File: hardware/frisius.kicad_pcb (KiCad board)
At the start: 2 copper layers, 40 x 60 mm, 17 parts

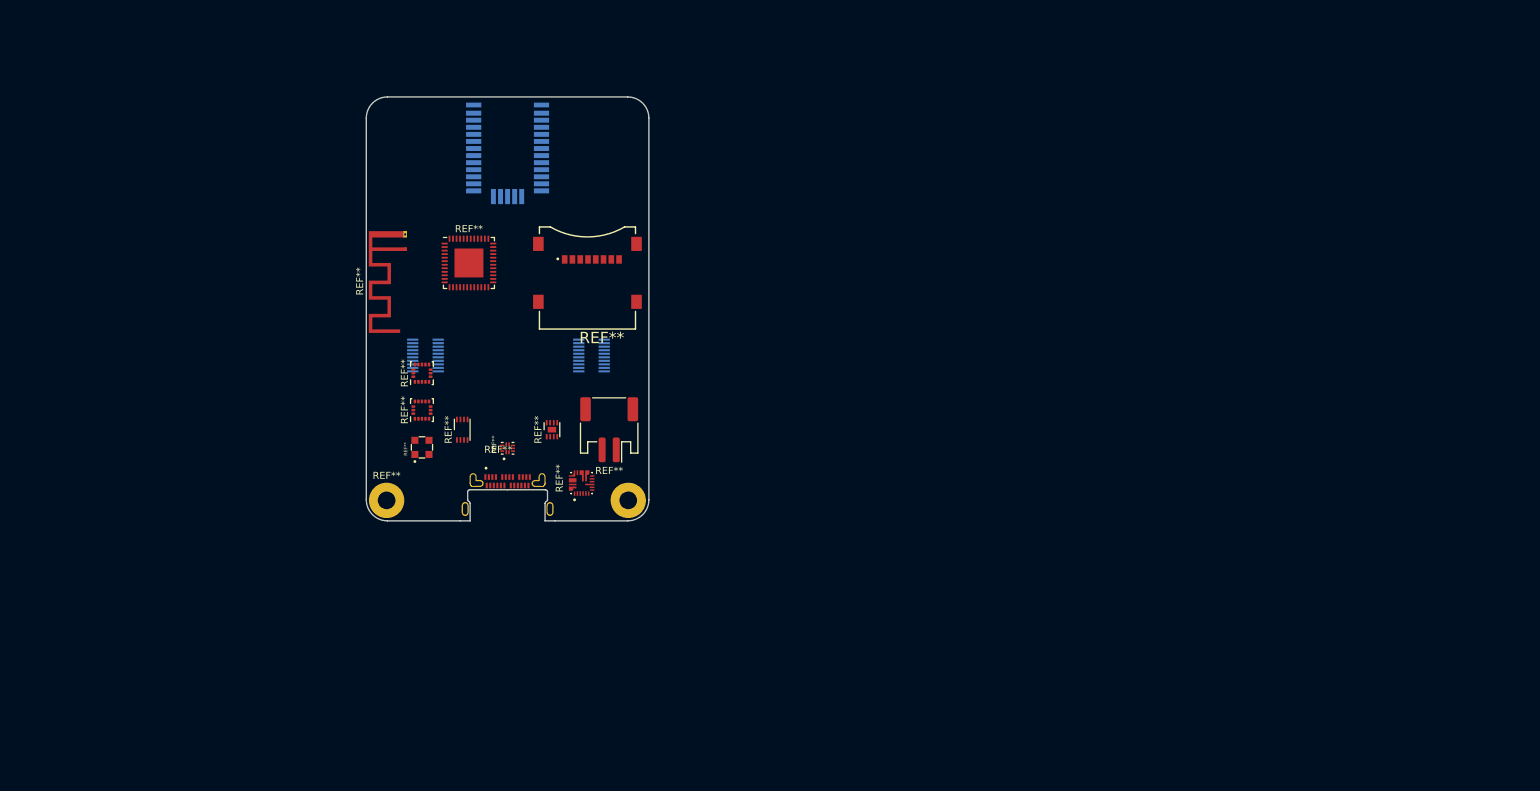
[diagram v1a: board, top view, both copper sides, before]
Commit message: checking footprint assignment, added current sense pac1934 for dev
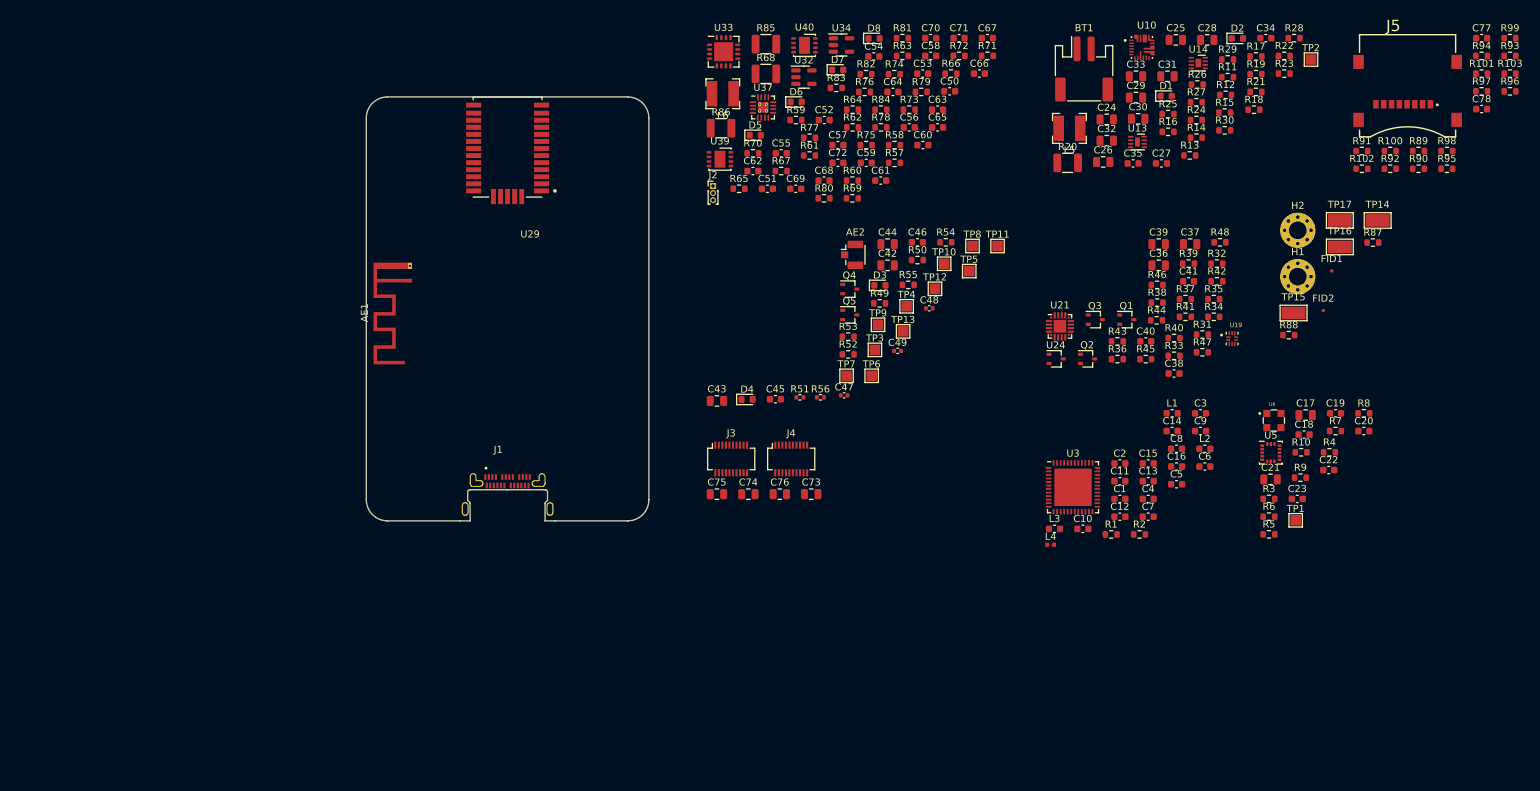
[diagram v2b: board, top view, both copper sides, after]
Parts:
- removed ?: , 
- removed REF**: DFN-8-1EP_3x2mm_P0.5mm_EP1.7x1.4mm, Package_DFN_QFN:DFN-8-1EP_3x2mm_P0.5mm_EP1.7x1.4mm
- removed REF** (x2): LGA-16_3x3mm_P0.5mm_LayoutBorder3x5y, Package_LGA:LGA-16_3x3mm_P0.5mm_LayoutBorder3x5y
- removed REF**: VQFN-48-1EP_7x7mm_P0.5mm_EP4.1x4.1mm, Package_DFN_QFN:VQFN-48-1EP_7x7mm_P0.5mm_EP4.1x4.1mm
- removed REF**: IC_MAX77751CEFG+, Package_QFN_bt:FC2QFN-24-3x3_P0.4mm
- removed REF**: IC_FSUSB30UMX, Package_QFN_bt:UMLP-10-1.4x1.8_P0.4mm
- removed REF**: XCVR_L96-M33, Module_GPS_bt:Quectel_L96-M33
- removed REF** (x2): Hirose_DF12_DF12E3.0-20DP-0.5V_2x10_P0.50mm_Vertical, Connector_Hirose:Hirose_DF12_DF12E3.0-20DP-0.5V_2x10_P0.50mm_Vertical
- removed REF**: AMPHENOL_124019032112A, Connector_USB_bt:AMPHENOL_124019032112A
- removed REF**: Texas_SWRA117D_2.4GHz_Left, RF_Antenna:Texas_SWRA117D_2.4GHz_Left
- removed REF**: TDFN-8-1EP_2x2mm_P0.5mm_EP0.8x1.2mm, Package_DFN_QFN:TDFN-8-1EP_2x2mm_P0.5mm_EP0.8x1.2mm
- removed REF**: TE_MS563702BA03-50, Package_LGA_bt:TE_MS563702BA03-50
- removed REF**: GCT_MEM2067-02-180-00-A_REVB, Connector_uSD_bt:GCT_MEM2067-02-180-00-A_REVB
- removed REF**: JST_PH_S2B-PH-SM4-TB_1x02-1MP_P2.00mm_Horizontal, Connector_JST:JST_PH_S2B-PH-SM4-TB_1x02-1MP_P2.00mm_Horizontal
- removed REF**: MountingHole_2.5mm_Pad, MountingHole:MountingHole_2.5mm_Pad
- added AE1: 2.4G, RF_Antenna:Texas_SWRA117D_2.4GHz_Left, F.Cu at (120.8, 59.9)
- added AE2: GPS_EXT, Connector_Coaxial:U.FL_Hirose_U.FL-R-SMT-1_Vertical, F.Cu at (183.4, 56.2)
- added BT1: JST-PH-2, Connector_JST:JST_PH_S2B-PH-SM4-TB_1x02-1MP_P2.00mm_Horizontal, F.Cu at (216.2, 29.9)
- added C1: 0.1u, Capacitor_SMD:C_0603_1608Metric, F.Cu at (221.3, 90.8)
- added C10: 4.7u, Capacitor_SMD:C_0603_1608Metric, F.Cu at (216.0, 95.0)
- added C11: 4.7u, Capacitor_SMD:C_0603_1608Metric, F.Cu at (221.3, 88.3)
- added C12: 4.7u, Capacitor_SMD:C_0603_1608Metric, F.Cu at (221.3, 93.3)
- added C13: 4.7u, Capacitor_SMD:C_0603_1608Metric, F.Cu at (225.3, 88.3)
- added C14: 4.7u, Capacitor_SMD:C_0603_1608Metric, F.Cu at (228.7, 81.2)
- added C15: 0.1u, Capacitor_SMD:C_0603_1608Metric, F.Cu at (225.3, 85.8)
- added C16: 0.1u, Capacitor_SMD:C_0603_1608Metric, F.Cu at (229.3, 86.2)
- added C17: 4.7u, Capacitor_SMD:C_0805_2012Metric, F.Cu at (247.6, 78.9)
- added C18: 0.1u, Capacitor_SMD:C_0603_1608Metric, F.Cu at (247.3, 81.7)
- added C19: 0.1u, Capacitor_SMD:C_0603_1608Metric, F.Cu at (251.8, 78.7)
- added C2: 0.1u, Capacitor_SMD:C_0603_1608Metric, F.Cu at (221.3, 85.8)
- added C20: 0.1u, Capacitor_SMD:C_0603_1608Metric, F.Cu at (255.8, 81.2)
- added C21: 4.7u, Capacitor_SMD:C_0805_2012Metric, F.Cu at (242.6, 88.0)
- added C22: 0.1u, Capacitor_SMD:C_0603_1608Metric, F.Cu at (250.8, 86.7)
- added C23: 0.1u, Capacitor_SMD:C_0603_1608Metric, F.Cu at (246.4, 90.8)
- added C24: 4.7u, Capacitor_SMD:C_0805_2012Metric, F.Cu at (219.4, 37.1)
- added C25: 4.7u, Capacitor_SMD:C_0805_2012Metric, F.Cu at (229.2, 25.8)
- added C26: 4.7u, Capacitor_SMD:C_0805_2012Metric, F.Cu at (218.9, 43.1)
- added C27: 0.1u, Capacitor_SMD:C_0603_1608Metric, F.Cu at (227.2, 43.3)
- added C28: 4.7u, Capacitor_SMD:C_0805_2012Metric, F.Cu at (233.7, 25.8)
- added C29: 10u, Capacitor_SMD:C_0805_2012Metric, F.Cu at (223.6, 34.0)
- added C3: DNF, Capacitor_SMD:C_0603_1608Metric, F.Cu at (232.7, 78.7)
- added C30: 10u, Capacitor_SMD:C_0805_2012Metric, F.Cu at (223.9, 37.0)
- added C31: 10u, Capacitor_SMD:C_0805_2012Metric, F.Cu at (228.0, 31.0)
- added C32: 10u, Capacitor_SMD:C_0805_2012Metric, F.Cu at (219.4, 40.1)
- added C33: 10u, Capacitor_SMD:C_0805_2012Metric, F.Cu at (223.6, 31.0)
- added C34: 0.1u, Capacitor_SMD:C_0603_1608Metric, F.Cu at (241.9, 25.6)
- added C35: 0.1u, Capacitor_SMD:C_0603_1608Metric, F.Cu at (223.2, 43.3)
- added C36: 4.7u, Capacitor_SMD:C_0805_2012Metric, F.Cu at (226.8, 57.7)
- added C37: 4.7u, Capacitor_SMD:C_0805_2012Metric, F.Cu at (231.2, 54.7)
- added C38: 0.1u, Capacitor_SMD:C_0603_1608Metric, F.Cu at (228.9, 73.0)
- added C39: 4.7u, Capacitor_SMD:C_0805_2012Metric, F.Cu at (226.8, 54.7)
- added C4: DNF, Capacitor_SMD:C_0603_1608Metric, F.Cu at (225.3, 90.8)
- added C40: 0.1u, Capacitor_SMD:C_0603_1608Metric, F.Cu at (224.9, 68.5)
- added C41: 0.1u, Capacitor_SMD:C_0603_1608Metric, F.Cu at (231.0, 60.0)
- added C42: 4.7u, Capacitor_SMD:C_0805_2012Metric, F.Cu at (188.4, 57.7)
- added C43: 4.7u, Capacitor_SMD:C_0805_2012Metric, F.Cu at (164.2, 76.9)
- added C44: 4.7u, Capacitor_SMD:C_0805_2012Metric, F.Cu at (188.4, 54.7)
- added C45: 0.1u, Capacitor_SMD:C_0603_1608Metric, F.Cu at (172.5, 76.7)
- added C46: 0.1u, Capacitor_SMD:C_0603_1608Metric, F.Cu at (192.6, 54.5)
- added C47: DNF, Capacitor_SMD:C_0402_1005Metric, F.Cu at (182.3, 76.1)
- added C48: 100p, Capacitor_SMD:C_0402_1005Metric, F.Cu at (194.3, 63.8)
- added C49: DNF, Capacitor_SMD:C_0402_1005Metric, F.Cu at (189.8, 69.8)
- added C5: 0.1u, Capacitor_SMD:C_0603_1608Metric, F.Cu at (229.3, 88.7)
- added C50: 4.7u, Capacitor_SMD:C_0603_1608Metric, F.Cu at (197.2, 33.1)
- added C51: 4.7u, Capacitor_SMD:C_0603_1608Metric, F.Cu at (171.4, 46.9)
- added C52: 4.7u, Capacitor_SMD:C_0603_1608Metric, F.Cu at (179.4, 37.2)
- added C53: 4.7u, Capacitor_SMD:C_0603_1608Metric, F.Cu at (193.4, 30.6)
- added C54: 4.7u, Capacitor_SMD:C_0603_1608Metric, F.Cu at (186.4, 28.2)
- added C55: 4.7u, Capacitor_SMD:C_0603_1608Metric, F.Cu at (173.3, 41.9)
- added C56: 4.7u, Capacitor_SMD:C_0603_1608Metric, F.Cu at (191.5, 38.2)
- added C57: 0.1u, Capacitor_SMD:C_0603_1608Metric, F.Cu at (181.4, 40.7)
- added C58: 4.7u, Capacitor_SMD:C_0603_1608Metric, F.Cu at (194.5, 28.1)
- added C59: 0.1u, Capacitor_SMD:C_0603_1608Metric, F.Cu at (185.4, 43.2)
- added C6: 0.1u, Capacitor_SMD:C_0603_1608Metric, F.Cu at (233.3, 86.2)
- added C60: 0.1u, Capacitor_SMD:C_0603_1608Metric, F.Cu at (193.4, 40.7)
- added C61: 4.7u, Capacitor_SMD:C_0603_1608Metric, F.Cu at (187.4, 45.7)
- added C62: 0.1u, Capacitor_SMD:C_0603_1608Metric, F.Cu at (169.3, 44.4)
- added C63: 4.7u, Capacitor_SMD:C_0603_1608Metric, F.Cu at (195.5, 35.7)
- added C64: 4.7u, Capacitor_SMD:C_0603_1608Metric, F.Cu at (189.2, 33.2)
- added C65: 0.1u, Capacitor_SMD:C_0603_1608Metric, F.Cu at (195.5, 38.2)
- added C66: 0.1u, Capacitor_SMD:C_0603_1608Metric, F.Cu at (201.4, 30.6)
- added C67: 4.7u, Capacitor_SMD:C_0603_1608Metric, F.Cu at (202.5, 25.6)
- added C68: 4.7u, Capacitor_SMD:C_0603_1608Metric, F.Cu at (179.4, 45.7)
- added C69: 4.7u, Capacitor_SMD:C_0603_1608Metric, F.Cu at (175.4, 46.9)
- added C7: 0.1u, Capacitor_SMD:C_0603_1608Metric, F.Cu at (225.3, 93.3)
- added C70: 4.7u, Capacitor_SMD:C_0603_1608Metric, F.Cu at (194.5, 25.6)
- added C71: 4.7u, Capacitor_SMD:C_0603_1608Metric, F.Cu at (198.5, 25.6)
- added C72: 4.7u, Capacitor_SMD:C_0603_1608Metric, F.Cu at (181.4, 43.2)
- added C73: 4.7u, Capacitor_SMD:C_0805_2012Metric, F.Cu at (177.6, 90.1)
- added C74: 4.7u, Capacitor_SMD:C_0805_2012Metric, F.Cu at (168.7, 90.1)
- added C75: 4.7u, Capacitor_SMD:C_0805_2012Metric, F.Cu at (164.2, 90.1)
- added C76: 4.7u, Capacitor_SMD:C_0805_2012Metric, F.Cu at (173.2, 90.1)
- added C77: 0.1u, Capacitor_SMD:C_0603_1608Metric, F.Cu at (272.5, 25.6)
- added C78: 4.7u, Capacitor_SMD:C_0603_1608Metric, F.Cu at (272.5, 35.6)
- added C8: 0.1u, Capacitor_SMD:C_0603_1608Metric, F.Cu at (229.3, 83.7)
- added C9: 0.1u, Capacitor_SMD:C_0603_1608Metric, F.Cu at (232.7, 81.2)
- added D1: LED_Small_Filled, LED_SMD:LED_0603_1608Metric, F.Cu at (227.8, 33.8)
- added D2: LED_Small_Filled, LED_SMD:LED_0603_1608Metric, F.Cu at (237.9, 25.6)
- added D3: LED_Small_Filled, LED_SMD:LED_0603_1608Metric, F.Cu at (187.3, 60.6)
- added D4: LED_Small_Filled, LED_SMD:LED_0603_1608Metric, F.Cu at (168.5, 76.7)
- added D5: MBR0540, Diode_SMD:D_0603_1608Metric, F.Cu at (169.7, 39.3)
- added D6: LED_Small_Filled, LED_SMD:LED_0603_1608Metric, F.Cu at (175.5, 34.6)
- added D7: LED_Small_Filled, LED_SMD:LED_0603_1608Metric, F.Cu at (181.3, 30.1)
- added D8: LED_Small_Filled, LED_SMD:LED_0603_1608Metric, F.Cu at (186.5, 25.6)
- added FID1: TR, Fiducial:Fiducial_0.5mm_Mask1.5mm, F.Cu at (251.3, 58.5)
- added FID2: BR, Fiducial:Fiducial_0.5mm_Mask1.5mm, F.Cu at (250.1, 64.1)
- added H1: BL, MountingHole:MountingHole_2.5mm_Pad_Via, F.Cu at (246.5, 59.3)
- added H2: BR, MountingHole:MountingHole_2.5mm_Pad_Via, F.Cu at (246.5, 52.8)
- added J1: USB_C_Receptacle, bt_Connector_USB:AMPHENOL_124019032112A, F.Cu at (134.6, 91.4)
- added J2: Conn_01x03, Connector_PinHeader_1.00mm:PinHeader_1x03_P1.00mm_Vertical, F.Cu at (163.7, 46.5)
- added J3: Conn_02x10_Odd_Even_Shielded, Connector_Molex:Molex_SlimStack_55560-0201_2x10_P0.50mm_Vertical, F.Cu at (166.3, 85.1)
- added J4: Conn_02x10_Odd_Even_Shielded, Connector_Molex:Molex_SlimStack_55560-0201_2x10_P0.50mm_Vertical, F.Cu at (174.8, 85.1)
- added J5: MEM2067, bt_Connector_uSD:GCT_MEM2067-02-180-00-A_REVB, F.Cu at (262.0, 32.3)
- added L1: L_Small, Inductor_SMD:L_0603_1608Metric, F.Cu at (228.7, 78.7)
- added L2: 0R, Inductor_SMD:L_0603_1608Metric, F.Cu at (233.3, 83.7)
- added L3: 0R, Inductor_SMD:L_0603_1608Metric, F.Cu at (212.0, 95.0)
- added L4: L_Small, Inductor_SMD:L_0402_1005Metric, F.Cu at (211.5, 97.3)
- added L5: 0.47u, Inductor_SMD:L_Bourns-SRN4018, F.Cu at (214.1, 38.4)
- added L6: L_Small, Inductor_SMD:L_Bourns-SRN4018, F.Cu at (165.1, 33.5)
- added Q1: Q_NMOS_DGS, Package_TO_SOT_SMD:SOT-323_SC-70, F.Cu at (222.2, 65.4)
- added Q2: BC817W, Package_TO_SOT_SMD:SOT-323_SC-70, F.Cu at (216.7, 71.0)
- added Q3: BC817W, Package_TO_SOT_SMD:SOT-323_SC-70, F.Cu at (217.8, 65.4)
- added Q4: BC817W, Package_TO_SOT_SMD:SOT-323_SC-70, F.Cu at (183.1, 61.1)
- added Q5: BC817W, Package_TO_SOT_SMD:SOT-323_SC-70, F.Cu at (183.1, 64.8)
- added R1: 10k, Resistor_SMD:R_0603_1608Metric, F.Cu at (220.1, 95.8)
- added R10: 10k, Resistor_SMD:R_0603_1608Metric, F.Cu at (246.9, 84.2)
- added R100: 10k, Resistor_SMD:R_0603_1608Metric, F.Cu at (259.5, 41.6)
- added R101: 10k, Resistor_SMD:R_0603_1608Metric, F.Cu at (272.5, 30.6)
- added R102: 10k, Resistor_SMD:R_0603_1608Metric, F.Cu at (255.5, 44.1)
- added R103: 0, Resistor_SMD:R_0603_1608Metric, F.Cu at (276.5, 30.6)
- added R11: 0, Resistor_SMD:R_0603_1608Metric, F.Cu at (236.5, 31.1)
- added R12: 0, Resistor_SMD:R_0603_1608Metric, F.Cu at (236.2, 33.6)
- added R13: 100k, Resistor_SMD:R_0603_1608Metric, F.Cu at (231.2, 42.2)
- added R14: 1k, Resistor_SMD:R_0603_1608Metric, F.Cu at (232.1, 39.7)
- added R15: 100k, Resistor_SMD:R_0603_1608Metric, F.Cu at (236.1, 36.1)
- added R16: 1k, Resistor_SMD:R_0603_1608Metric, F.Cu at (228.1, 38.8)
- added R17: 14k, Resistor_SMD:R_0603_1608Metric, F.Cu at (240.5, 28.2)
- added R18: 14k, Resistor_SMD:R_0603_1608Metric, F.Cu at (240.3, 35.7)
- added R19: 0, Resistor_SMD:R_0603_1608Metric, F.Cu at (240.5, 30.7)
- added R2: 10k, Resistor_SMD:R_0603_1608Metric, F.Cu at (224.1, 95.8)
- added R20: 10m, Resistor_SMD:R_1210_3225Metric, F.Cu at (213.9, 43.2)
- added R21: 100, Resistor_SMD:R_0603_1608Metric, F.Cu at (240.5, 33.2)
- added R22: 4.7k, Resistor_SMD:R_0603_1608Metric, F.Cu at (244.6, 28.1)
- added R23: 4.7k, Resistor_SMD:R_0603_1608Metric, F.Cu at (244.6, 30.6)
- added R24: 4.7k, Resistor_SMD:R_0603_1608Metric, F.Cu at (232.1, 37.2)
- added R25: 100k, Resistor_SMD:R_0603_1608Metric, F.Cu at (228.1, 36.3)
- added R26: 100k, Resistor_SMD:R_0603_1608Metric, F.Cu at (232.2, 32.1)
- added R27: 100k, Resistor_SMD:R_0603_1608Metric, F.Cu at (232.1, 34.6)
- added R28: 100k, Resistor_SMD:R_0603_1608Metric, F.Cu at (245.9, 25.6)
- added R29: 100k, Resistor_SMD:R_0603_1608Metric, F.Cu at (236.5, 28.6)
- added R3: 10k, Resistor_SMD:R_0603_1608Metric, F.Cu at (242.4, 90.8)
- added R30: 100k, Resistor_SMD:R_0603_1608Metric, F.Cu at (236.1, 38.6)
- added R31: 0, Resistor_SMD:R_0603_1608Metric, F.Cu at (233.0, 67.5)
- added R32: 22, Resistor_SMD:R_0603_1608Metric, F.Cu at (235.0, 57.5)
- added R33: 22, Resistor_SMD:R_0603_1608Metric, F.Cu at (228.9, 70.5)
- added R34: 100k, Resistor_SMD:R_0603_1608Metric, F.Cu at (234.6, 65.0)
- added R35: 0, Resistor_SMD:R_0603_1608Metric, F.Cu at (234.6, 62.5)
- added R36: 100k, Resistor_SMD:R_0603_1608Metric, F.Cu at (220.9, 71.0)
- added R37: 0, Resistor_SMD:R_0603_1608Metric, F.Cu at (230.6, 62.5)
- added R38: 0, Resistor_SMD:R_0603_1608Metric, F.Cu at (226.6, 63.0)
- added R39: 22, Resistor_SMD:R_0603_1608Metric, F.Cu at (231.0, 57.5)
- added R4: 4.7k, Resistor_SMD:R_0603_1608Metric, F.Cu at (250.9, 84.2)
- added R40: 22, Resistor_SMD:R_0603_1608Metric, F.Cu at (228.9, 68.0)
- added R41: 10k, Resistor_SMD:R_0603_1608Metric, F.Cu at (230.6, 65.0)
- added R42: 0, Resistor_SMD:R_0603_1608Metric, F.Cu at (235.0, 60.0)
- added R43: 100k, Resistor_SMD:R_0603_1608Metric, F.Cu at (220.9, 68.5)
- added R44: 0, Resistor_SMD:R_0603_1608Metric, F.Cu at (226.5, 65.5)
- added R45: 0, Resistor_SMD:R_0603_1608Metric, F.Cu at (224.9, 71.0)
- added R46: 100k, Resistor_SMD:R_0603_1608Metric, F.Cu at (226.6, 60.5)
- added R47: 10k, Resistor_SMD:R_0603_1608Metric, F.Cu at (233.0, 70.0)
- added R48: 10k, Resistor_SMD:R_0603_1608Metric, F.Cu at (235.4, 54.5)
- added R49: 1k, Resistor_SMD:R_0603_1608Metric, F.Cu at (187.3, 63.1)
- added R5: 4.7k, Resistor_SMD:R_0603_1608Metric, F.Cu at (242.4, 95.8)
- added R50: 1k, Resistor_SMD:R_0603_1608Metric, F.Cu at (192.6, 57.0)
- added R51: 0, Resistor_SMD:R_0402_1005Metric, F.Cu at (176.0, 76.4)
- added R52: 22, Resistor_SMD:R_0603_1608Metric, F.Cu at (182.8, 70.3)
- added R53: 22, Resistor_SMD:R_0603_1608Metric, F.Cu at (182.8, 67.8)
- added R54: 22, Resistor_SMD:R_0603_1608Metric, F.Cu at (196.6, 54.5)
- added R55: 22, Resistor_SMD:R_0603_1608Metric, F.Cu at (191.3, 60.5)
- added R56: 0, Resistor_SMD:R_0402_1005Metric, F.Cu at (178.9, 76.4)
- added R57: 4.7k, Resistor_SMD:R_0603_1608Metric, F.Cu at (189.4, 43.2)
- added R58: 4.7k, Resistor_SMD:R_0603_1608Metric, F.Cu at (189.4, 40.7)
- added R59: 10k, Resistor_SMD:R_0603_1608Metric, F.Cu at (175.4, 37.2)
- added R6: 4.7k, Resistor_SMD:R_0603_1608Metric, F.Cu at (242.4, 93.3)
- added R60: 0, Resistor_SMD:R_0603_1608Metric, F.Cu at (183.4, 45.7)
- added R61: 0, Resistor_SMD:R_0603_1608Metric, F.Cu at (177.4, 42.2)
- added R62: 0, Resistor_SMD:R_0603_1608Metric, F.Cu at (183.4, 38.2)
- added R63: 10k, Resistor_SMD:R_0603_1608Metric, F.Cu at (190.5, 28.1)
- added R64: 0, Resistor_SMD:R_0603_1608Metric, F.Cu at (183.4, 35.7)
- added R65: 0, Resistor_SMD:R_0603_1608Metric, F.Cu at (167.4, 46.9)
- added R66: 10k, Resistor_SMD:R_0603_1608Metric, F.Cu at (197.4, 30.6)
- added R67: 10k, Resistor_SMD:R_0603_1608Metric, F.Cu at (173.3, 44.4)
- added R68: 10m, Resistor_SMD:R_1210_3225Metric, F.Cu at (171.2, 30.6)
- added R69: 10k, Resistor_SMD:R_0603_1608Metric, F.Cu at (183.4, 48.2)
- added R7: 10k, Resistor_SMD:R_0603_1608Metric, F.Cu at (251.8, 81.2)
- added R70: 10k, Resistor_SMD:R_0603_1608Metric, F.Cu at (169.3, 41.9)
- added R71: 10k, Resistor_SMD:R_0603_1608Metric, F.Cu at (202.5, 28.1)
- added R72: 0, Resistor_SMD:R_0603_1608Metric, F.Cu at (198.5, 28.1)
- added R73: 180k, Resistor_SMD:R_0603_1608Metric, F.Cu at (191.5, 35.7)
- added R74: 10k, Resistor_SMD:R_0603_1608Metric, F.Cu at (189.4, 30.7)
- added R75: 10k, Resistor_SMD:R_0603_1608Metric, F.Cu at (185.4, 40.7)
- added R76: 1k, Resistor_SMD:R_0603_1608Metric, F.Cu at (185.2, 33.2)
- added R77: 10k, Resistor_SMD:R_0603_1608Metric, F.Cu at (177.4, 39.7)
- added R78: 10k, Resistor_SMD:R_0603_1608Metric, F.Cu at (187.5, 38.2)
- added R79: 0, Resistor_SMD:R_0603_1608Metric, F.Cu at (193.2, 33.2)
- added R8: 10k, Resistor_SMD:R_0603_1608Metric, F.Cu at (255.8, 78.7)
- added R80: 10k, Resistor_SMD:R_0603_1608Metric, F.Cu at (179.4, 48.2)
- added R81: 0, Resistor_SMD:R_0603_1608Metric, F.Cu at (190.5, 25.6)
- added R82: 1k, Resistor_SMD:R_0603_1608Metric, F.Cu at (185.3, 30.7)
- added R83: 10K, Resistor_SMD:R_0603_1608Metric, F.Cu at (181.1, 32.6)
- added R84: 1k, Resistor_SMD:R_0603_1608Metric, F.Cu at (187.5, 35.7)
- added R85: 10m, Resistor_SMD:R_1210_3225Metric, F.Cu at (171.2, 26.4)
- added R86: 10m, Resistor_SMD:R_1210_3225Metric, F.Cu at (164.8, 38.3)
- added R87: 0, Resistor_SMD:R_0603_1608Metric, F.Cu at (257.1, 54.5)
- added R88: 0, Resistor_SMD:R_0603_1608Metric, F.Cu at (245.2, 67.6)
- added R89: 22, Resistor_SMD:R_0603_1608Metric, F.Cu at (263.6, 41.6)
- added R9: 10k, Resistor_SMD:R_0603_1608Metric, F.Cu at (246.8, 87.8)
- added R90: 22, Resistor_SMD:R_0603_1608Metric, F.Cu at (263.6, 44.1)
- added R91: 22, Resistor_SMD:R_0603_1608Metric, F.Cu at (255.5, 41.6)
- added R92: 22, Resistor_SMD:R_0603_1608Metric, F.Cu at (259.5, 44.1)
- added R93: 22, Resistor_SMD:R_0603_1608Metric, F.Cu at (276.5, 28.1)
- added R94: 22, Resistor_SMD:R_0603_1608Metric, F.Cu at (272.5, 28.1)
- added R95: 22, Resistor_SMD:R_0603_1608Metric, F.Cu at (267.6, 44.1)
- added R96: 10k, Resistor_SMD:R_0603_1608Metric, F.Cu at (276.5, 33.1)
- added R97: 10k, Resistor_SMD:R_0603_1608Metric, F.Cu at (272.5, 33.1)
- added R98: 10k, Resistor_SMD:R_0603_1608Metric, F.Cu at (267.6, 41.6)
- added R99: 10k, Resistor_SMD:R_0603_1608Metric, F.Cu at (276.5, 25.6)
- added TP1: IMU_ALERT, TestPoint:TestPoint_Pad_1.5x1.5mm, F.Cu at (246.2, 93.8)
- added TP10: L96_SCL, TestPoint:TestPoint_Pad_1.5x1.5mm, F.Cu at (196.4, 57.5)
- added TP11: GPS_FORCE_ON, TestPoint:TestPoint_Pad_1.5x1.5mm, F.Cu at (204.0, 55.0)
- added TP12: L96_TXD, TestPoint:TestPoint_Pad_1.5x1.5mm, F.Cu at (195.1, 61.1)
- added TP13: L96_RXD, TestPoint:TestPoint_Pad_1.5x1.5mm, F.Cu at (190.6, 67.1)
- added TP14: GND, TestPoint:TestPoint_Keystone_5015_Micro-Minature, F.Cu at (257.8, 51.4)
- added TP15: GND, TestPoint:TestPoint_Keystone_5015_Micro-Minature, F.Cu at (245.9, 64.5)
- added TP16: GND, TestPoint:TestPoint_Keystone_5015_Micro-Minature, F.Cu at (252.4, 55.1)
- added TP17: GND, TestPoint:TestPoint_Keystone_5015_Micro-Minature, F.Cu at (252.4, 51.4)
- added TP2: FG_ALERT, TestPoint:TestPoint_Pad_1.5x1.5mm, F.Cu at (248.3, 28.6)
- added TP3: L96_JAM, TestPoint:TestPoint_Pad_1.5x1.5mm, F.Cu at (186.6, 69.7)
- added TP4: L96_JAM, TestPoint:TestPoint_Pad_1.5x1.5mm, F.Cu at (191.1, 63.5)
- added TP5: L96_JAM, TestPoint:TestPoint_Pad_1.5x1.5mm, F.Cu at (200.0, 58.5)
- added TP6: L96_GEO, TestPoint:TestPoint_Pad_1.5x1.5mm, F.Cu at (186.2, 73.4)
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
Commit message: hardware update
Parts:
- removed AE2: GPS_EXT, Connector_Coaxial:U.FL_Hirose_U.FL-R-SMT-1_Vertical
- removed C55, C56, C58, C61, C63, C64, C67, C68, C69, C70, C71, C72, C78: 4.7u, Capacitor_SMD:C_0603_1608Metric
- removed C57, C59, C60, C62, C65, C66, C77: 0.1u, Capacitor_SMD:C_0603_1608Metric
- removed C73, C74, C75, C76: 4.7u, Capacitor_SMD:C_0805_2012Metric
- removed FID1: TR, Fiducial:Fiducial_0.5mm_Mask1.5mm
- removed FID2: BR, Fiducial:Fiducial_0.5mm_Mask1.5mm
- removed the J3 at (166.3, 85.1)
- removed J5: MEM2067, bt_Connector_uSD:GCT_MEM2067-02-180-00-A_REVB
- removed L5: 0.47u, Inductor_SMD:L_Bourns-SRN4018
- removed L6: L_Small, Inductor_SMD:L_Bourns-SRN4018
- removed Q5: BC817W, Package_TO_SOT_SMD:SOT-323_SC-70
- removed R100, R101, R102, R59, R63, R66, R67, R69, R70, R71, R74, R75, R77, R78, R80, R96, R97, R98, R99: 10k, Resistor_SMD:R_0603_1608Metric
- removed R103, R60, R61, R62, R64, R65, R72, R79, R81, R87, R88: 0, Resistor_SMD:R_0603_1608Metric
- removed R68, R85, R86: 10m, Resistor_SMD:R_1210_3225Metric
- removed R73: 180k, Resistor_SMD:R_0603_1608Metric
- removed R76, R82, R84: 1k, Resistor_SMD:R_0603_1608Metric
- removed R83: 10K, Resistor_SMD:R_0603_1608Metric
- removed R89, R90, R91, R92, R93, R94, R95: 22, Resistor_SMD:R_0603_1608Metric
- removed TP10: L96_SCL, TestPoint:TestPoint_Pad_1.5x1.5mm
- removed TP11: GPS_FORCE_ON, TestPoint:TestPoint_Pad_1.5x1.5mm
- removed TP12: L96_TXD, TestPoint:TestPoint_Pad_1.5x1.5mm
- removed TP13: L96_RXD, TestPoint:TestPoint_Pad_1.5x1.5mm
- removed TP14, TP15, TP16, TP17: GND, TestPoint:TestPoint_Keystone_5015_Micro-Minature
- removed TP2: FG_ALERT, TestPoint:TestPoint_Pad_1.5x1.5mm
- removed TP3, TP4, TP5: L96_JAM, TestPoint:TestPoint_Pad_1.5x1.5mm
- removed TP6: L96_GEO, TestPoint:TestPoint_Pad_1.5x1.5mm
- removed TP7: GPS_RESET, TestPoint:TestPoint_Pad_1.5x1.5mm
- removed TP8: L96_SDA, TestPoint:TestPoint_Pad_1.5x1.5mm
- removed TP9: GPS_EXTINT, TestPoint:TestPoint_Pad_1.5x1.5mm
- removed U19: FSUSB30UMX, bt_Package_QFN:UMLP-10-1.4x1.8_P0.4mm
- removed U21: CP2102N-Axx-xQFN24, Package_DFN_QFN:SiliconLabs_QFN-20-1EP_3x3mm_P0.5mm_EP1.8x1.8mm
- removed U24: 74LVC2G126GT,115, Package_TO_SOT_SMD:SOT-323_SC-70
- removed U29: L96-M33, bt_Module_GPS:Quectel_L96-M33
- removed U32, U34: LDK220M-R, Package_TO_SOT_SMD:SOT-23-5
- removed U33: PAC1934x-xJQ, Package_DFN_QFN:UQFN-16-1EP_4x4mm_P0.65mm_EP2.7x2.7mm
- removed U37: PM8903A, Package_DFN_QFN:VQFN-16-1EP_3x3mm_P0.5mm_EP1.45x1.45mm_ThermalVias
- removed U39, U40: NCV8187AMLExCG, Package_DFN_QFN:DFN-8-1EP_3x3mm_P0.65mm_EP1.55x2.4mm
- added J1: Conn_02x10_Odd_Even_Shielded, Connector_Molex:Molex_SlimStack_55560-0201_2x10_P0.50mm_Vertical, B.Cu at (121.0, 63.9)
- added U1: ESP32-PICO-V3-02, Package_DFN_QFN:QFN-48-1EP_7x7mm_P0.5mm_EP5.3x5.3mm, F.Cu at (137.4, 47.1)
- added U11: 74LVC2G126GT,115, Package_SON:X2SON-8_1.4x1mm_P0.35mm, F.Cu at (122.2, 86.3)
- added U12: RT5789, Package_DFN_QFN:DFN-10-1EP_3x3mm_P0.5mm_EP1.55x2.48mm, F.Cu at (167.4, 56.9)
- added U15: AP228X4BSN, bt_Package_DFN:Diodes_UDFN2020-6, F.Cu at (174.0, 67.2)
- added U2: FXOS8700CQR1, Package_LGA:LGA-16_3x3mm_P0.5mm_LayoutBorder3x5y, F.Cu at (96.6, 61.0)
- added U4: L96-M33, bt_Module_GPS:Quectel_L96-M33, B.Cu at (134.8, 41.4)
- added U7: MAX17048G, Package_DFN_QFN:TDFN-8-1EP_2x2mm_P0.5mm_EP0.8x1.2mm, F.Cu at (152.1, 80.4)
- added U8: MAX8881EUT33+T, Package_TO_SOT_SMD:SOT-23-6, F.Cu at (99.5, 71.0)
- added U9: ISL54225, Package_DFN_QFN:DFN-10-1EP_3x3mm_P0.5mm_EP1.55x2.48mm, F.Cu at (134.6, 81.2)
- BT1: footprint Connector_JST:JST_PH_S2B-PH-SM4-TB_1x02-1MP_P2.00mm_Horizontal -> Connector_PinHeader_1.00mm:PinHeader_1x02_P1.00mm_Vertical
- C1, C2, C45, C8: value 0.1u -> 1u
- C10, C12, C13, C14, C50: value 4.7u -> 0.1u; footprint Capacitor_SMD:C_0603_1608Metric -> Capacitor_SMD:C_0402_1005Metric
- C15, C16, C19, C22, C38, C40, C41, C5, C6, C7, C9: footprint Capacitor_SMD:C_0603_1608Metric -> Capacitor_SMD:C_0402_1005Metric
- C17, C42: value 4.7u -> 0.1u; footprint Capacitor_SMD:C_0805_2012Metric -> Capacitor_SMD:C_0402_1005Metric
- C18, C20, C23, C34, C35, C46: value 0.1u -> 4.7u
- C21, C36, C39, C43: footprint Capacitor_SMD:C_0805_2012Metric -> Capacitor_SMD:C_0603_1608Metric
- C24, C25, C26, C28: value 4.7u -> 10u
- C27: value 0.1u -> 10u; footprint Capacitor_SMD:C_0603_1608Metric -> Capacitor_SMD:C_0805_2012Metric
- C29, C30: value 10u -> 0.1u; footprint Capacitor_SMD:C_0805_2012Metric -> Capacitor_SMD:C_0402_1005Metric
- C3: value DNF -> 0.1u; footprint Capacitor_SMD:C_0603_1608Metric -> Capacitor_SMD:C_0402_1005Metric
- C31, C32, C33: value 10u -> 4.7u; footprint Capacitor_SMD:C_0805_2012Metric -> Capacitor_SMD:C_0603_1608Metric
- C37, C44: value 4.7u -> 1u; footprint Capacitor_SMD:C_0805_2012Metric -> Capacitor_SMD:C_0603_1608Metric
- C4: value DNF -> 1u
- C47: value DNF -> 10p
- C48: value 100p -> 10u; footprint Capacitor_SMD:C_0402_1005Metric -> Capacitor_SMD:C_0805_2012Metric
- C49: value DNF -> 10u; footprint Capacitor_SMD:C_0402_1005Metric -> Capacitor_SMD:C_0805_2012Metric
- C51, C52: value 4.7u -> 10u; footprint Capacitor_SMD:C_0603_1608Metric -> Capacitor_SMD:C_0805_2012Metric
- C53: value 4.7u -> 0.1u
- D4: value LED_Small_Filled -> TVS; footprint LED_SMD:LED_0603_1608Metric -> Diode_SMD:D_SOD-523
- D5: value MBR0540 -> 3.3V; footprint Diode_SMD:D_0603_1608Metric -> Diode_SMD:D_SOD-523
- D6: value LED_Small_Filled -> MBR0540
- J2: value Conn_01x03 -> Conn_02x10_Odd_Even_Shielded; footprint Connector_PinHeader_1.00mm:PinHeader_1x03_P1.00mm_Vertical -> Connector_Molex:Molex_SlimStack_55560-0201_2x10_P0.50mm_Vertical; moved to B.Cu
- J4: value Conn_02x10_Odd_Even_Shielded -> MEM2067; footprint Connector_Molex:Molex_SlimStack_55560-0201_2x10_P0.50mm_Vertical -> bt_Connector_uSD:GCT_MEM2067-02-180-00-A_REVB
- L1: value L_Small -> 0; footprint Inductor_SMD:L_0603_1608Metric -> Resistor_SMD:R_0603_1608Metric
- L2: value 0R -> L_Small; footprint Inductor_SMD:L_0603_1608Metric -> Inductor_SMD:L_0402_1005Metric
- L3: value 0R -> 0.47u; footprint Inductor_SMD:L_0603_1608Metric -> Inductor_SMD:L_Wuerth_MAPI-2510
- L4: value L_Small -> 1u; footprint Inductor_SMD:L_0402_1005Metric -> Inductor_SMD:L_Wuerth_MAPI-2510
- Q2: value BC817W -> MBT2222ADW1T1; footprint Package_TO_SOT_SMD:SOT-323_SC-70 -> Package_TO_SOT_SMD:SOT-363_SC-70-6
- Q3, Q4: value BC817W -> Q_NMOS_DGS
- R1: value 10k -> 100k; footprint Resistor_SMD:R_0603_1608Metric -> Resistor_SMD:R_0402_1005Metric
- R10, R47, R48, R7, R8, R9: value 10k -> 22; footprint Resistor_SMD:R_0603_1608Metric -> Resistor_SMD:R_0402_1005Metric
- R11, R35, R38, R42: value 0 -> 100k; footprint Resistor_SMD:R_0603_1608Metric -> Resistor_SMD:R_0402_1005Metric
- R12, R44: value 0 -> 1k; footprint Resistor_SMD:R_0603_1608Metric -> Resistor_SMD:R_0402_1005Metric
- R13: value 100k -> 1k; footprint Resistor_SMD:R_0603_1608Metric -> Resistor_SMD:R_0402_1005Metric
- R14: value 1k -> 14k; footprint Resistor_SMD:R_0603_1608Metric -> Resistor_SMD:R_0402_1005Metric
- R15: value 100k -> 14k; footprint Resistor_SMD:R_0603_1608Metric -> Resistor_SMD:R_0402_1005Metric
- R16: value 1k -> 0; footprint Resistor_SMD:R_0603_1608Metric -> Resistor_SMD:R_0402_1005Metric
- R17: value 14k -> 10m; footprint Resistor_SMD:R_0603_1608Metric -> Resistor_SMD:R_0603_1608Metric_Pad0.98x0.95mm_HandSolder
- R18: value 14k -> 4.7k; footprint Resistor_SMD:R_0603_1608Metric -> Resistor_SMD:R_0402_1005Metric
- R19: value 0 -> 4.7k; footprint Resistor_SMD:R_0603_1608Metric -> Resistor_SMD:R_0402_1005Metric
- R2, R27, R28, R29, R34, R36, R4: footprint Resistor_SMD:R_0603_1608Metric -> Resistor_SMD:R_0402_1005Metric
- R20: value 10m -> 4.7k; footprint Resistor_SMD:R_1210_3225Metric -> Resistor_SMD:R_0402_1005Metric
- R21: value 100 -> 22; footprint Resistor_SMD:R_0603_1608Metric -> Resistor_SMD:R_0402_1005Metric
- R22: value 4.7k -> 22; footprint Resistor_SMD:R_0603_1608Metric -> Resistor_SMD:R_0402_1005Metric
- R23, R24: value 4.7k -> 100k; footprint Resistor_SMD:R_0603_1608Metric -> Resistor_SMD:R_0402_1005Metric
- R25, R26, R46: value 100k -> 22; footprint Resistor_SMD:R_0603_1608Metric -> Resistor_SMD:R_0402_1005Metric
- R3: value 10k -> 4.7k; footprint Resistor_SMD:R_0603_1608Metric -> Resistor_SMD:R_0402_1005Metric
- R30: value 100k -> 10k; footprint Resistor_SMD:R_0603_1608Metric -> Resistor_SMD:R_0402_1005Metric
- R31: value 0 -> 10k; footprint Resistor_SMD:R_0603_1608Metric -> Resistor_SMD:R_0402_1005Metric
- R32, R33: value 22 -> 100k; footprint Resistor_SMD:R_0603_1608Metric -> Resistor_SMD:R_0402_1005Metric
- R37: value 0 -> ?; footprint Resistor_SMD:R_0603_1608Metric -> Resistor_SMD:R_0402_1005Metric
- R39, R40: value 22 -> 10m; footprint Resistor_SMD:R_0603_1608Metric -> Resistor_SMD:R_0603_1608Metric_Pad0.98x0.95mm_HandSolder
- R41: value 10k -> 1k; footprint Resistor_SMD:R_0603_1608Metric -> Resistor_SMD:R_0402_1005Metric
- R43: value 100k -> 10m
- R45: value 0 -> 22; footprint Resistor_SMD:R_0603_1608Metric -> Resistor_SMD:R_0402_1005Metric
- R49, R50: value 1k -> 22; footprint Resistor_SMD:R_0603_1608Metric -> Resistor_SMD:R_0402_1005Metric
- R5: value 4.7k -> 1k; footprint Resistor_SMD:R_0603_1608Metric -> Resistor_SMD:R_0402_1005Metric
- R51: value 0 -> 22
- R52, R53, R54, R55: value 22 -> 10k; footprint Resistor_SMD:R_0603_1608Metric -> Resistor_SMD:R_0402_1005Metric
- R56: value 0 -> 10k
- R57, R58: value 4.7k -> 10k; footprint Resistor_SMD:R_0603_1608Metric -> Resistor_SMD:R_0402_1005Metric
- R6: value 4.7k -> 0; footprint Resistor_SMD:R_0603_1608Metric -> Resistor_SMD:R_0402_1005Metric
- TP1: value IMU_ALERT -> L96_FIX; footprint TestPoint:TestPoint_Pad_1.5x1.5mm -> TestPoint:TestPoint_Pad_D1.0mm
- U10: value MAX77751 -> CP2102N-Axx-xQFN24; footprint bt_Package_QFN:FC2QFN-24-3x3_P0.4mm -> Package_DFN_QFN:QFN-24-1EP_4x4mm_P0.5mm_EP2.6x2.6mm
- U13: value LM75B -> MAX8881EUT33+T; footprint Package_DFN_QFN:DFN-8-1EP_2x2mm_P0.5mm_EP0.7x1.3mm -> Package_TO_SOT_SMD:SOT-23-6
- U14: value MAX17048G -> PAC1934x-xJQ; footprint Package_DFN_QFN:TDFN-8-1EP_2x2mm_P0.5mm_EP0.8x1.2mm -> Package_DFN_QFN:UQFN-16-1EP_4x4mm_P0.65mm_EP2.7x2.7mm
- U3: value ESP32-PICO-V3-02 -> MS5637-02BA03; footprint Package_DFN_QFN:QFN-48-1EP_7x7mm_P0.5mm_EP5.3x5.3mm -> bt_Package_LGA:TE_MS563702BA03-50
- U5: value FXOS8700CQR1 -> MAX77751; footprint Package_LGA:LGA-16_3x3mm_P0.5mm_LayoutBorder3x5y -> bt_Package_QFN:FC2QFN-24-3x3_P0.4mm
- U6: value MS5637-02BA03 -> LM75B; footprint bt_Package_LGA:TE_MS563702BA03-50 -> Package_DFN_QFN:DFN-8-1EP_2x2mm_P0.5mm_EP0.7x1.3mm
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- renumbered J1 to J3
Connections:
- AE1 pad 1: GND -> Net-(AE1-Pad1)
- AE1 pad 2: Net-(AE1-Pad2) -> GND
- C10 pad 1: /Processor/3V3_ESP_BCKP_FILT -> Net-(AE1-Pad1)
- C11 pad 1: /Processor/3V3_ESP_CORE_FILT -> VDD_AUX_3V3
- C12 pad 1: /Processor/3V3_ESP_VDDA_FILT -> VDD_AUX_3V3
- C13 pad 1: /Processor/3V3_ESP_VDDA_FILT -> Net-(C13-Pad1)
- C15 pad 1: Net-(C15-Pad1) -> VDD_AUX_3V3
- C15 pad 2: GND -> Net-(C15-Pad2)
- C16 pad 1: Net-(AE1-Pad2) -> Net-(C16-Pad1)
- C17 pad 1: VDD_AUX_3V3 -> VCC_BKUP_3V3
- C19 pad 1: Net-(C19-Pad1) -> VDD_AUX_3V3
- C2 pad 1: /Processor/3V3_ESP_VDDA_FILT -> 3V3_CORE
- C20 pad 1: Net-(C20-Pad1) -> VBUS
- C21 pad 1: VDD_AUX_3V3 -> Net-(C21-Pad1)
- C21 pad 2: Net-(C21-Pad2) -> GND
- C22 pad 1: VDD_AUX_3V3 -> Net-(C22-Pad1)
- C22 pad 2: Net-(C21-Pad2) -> Net-(C22-Pad2)
- C24 pad 1: VBUS -> VBUS_OVP
- C25 pad 1: VBUS -> VDD_NVDC
- C26 pad 1: Net-(C26-Pad1) -> VBUS_OVP
- C27 pad 1: Net-(C27-Pad1) -> VDD_NVDC
- C27 pad 2: Net-(C27-Pad2) -> GND
- C28 pad 1: Net-(C28-Pad1) -> +BATT
- C29 pad 1: VBUS_OVP -> +BATT
- C29 pad 2: GND -> Net-(C29-Pad2)
- C3 pad 1: VCC_BKUP_3V3 -> /Processor/3V3_ESP_VDDA_FILT
- C30 pad 1: VDD_NVDC -> +BATT
- C31 pad 1: VBUS_OVP -> VCC_BKUP_3V3
- C32 pad 1: VDD_NVDC -> VDD_AUX_3V3
- C33 pad 1: +BATT -> VDD_NVDC
- C34 pad 1: +BATT -> VDD_NVDC
- C34 pad 2: Net-(C34-Pad2) -> GND
- C35 pad 1: +BATT -> VBUS
- C36 pad 1: Net-(C36-Pad1) -> VBUS
- C37 pad 1: Net-(C36-Pad1) -> VDD_NVDC
- C42 pad 1: VDD_AUX_3V3 -> GND
- C42 pad 2: GND -> VCC_BKUP_3V3
- C43 pad 1: VCC_BKUP_3V3 -> VDD_NVDC
- C44 pad 1: VDD_AUX_3V3 -> VDD_NVDC
- C45 pad 1: VCC_BKUP_3V3 -> VDD_NVDC
- C46 pad 1: VDD_AUX_3V3 -> Net-(C46-Pad1)
- C47 pad 1: /GPS/GPS_RF -> VDD_SYS_3V3
- C47 pad 2: GND -> Net-(C47-Pad2)
- C48 pad 1: /GPS/GPS_RF_PI -> VDD_SYS_3V3
- C48 pad 2: /GPS/GPS_RF_EXT -> GND
- C49 pad 1: /GPS/GPS_RF_PI -> VDD_SYS_3V3
- C5 pad 1: /Processor/3V3_ESP_VDDA_FILT -> 3V3_CORE
- C50 pad 1: VDD_NVDC -> GND
- C50 pad 2: GND -> VDD_SYS_3V3
- C52 pad 1: VDD_USB_3V3 -> Net-(C51-Pad1)
- C53 pad 1: VCC_BKUP_3V3 -> VDD_AUX_3V3
- C54 pad 1: VDD_NVDC -> VDD_AUX_3V3
- C54 pad 2: Net-(C54-Pad2) -> GND
- C7 pad 1: /Processor/3V3_ESP_BCKP_FILT -> 3V3_CORE
- C8 pad 1: /Processor/3V3_ESP_CORE_FILT -> Net-(C8-Pad1)
- C9 pad 1: /Processor/3V3_ESP_VDDA_FILT -> Net-(C9-Pad1)
- D1 pad 1: Net-(D1-Pad1) -> GND
- D1 pad 2: 3V3_CORE -> Net-(D1-Pad2)
- D3 pad 2: Net-(D3-Pad2) -> 3V3_CORE
- D4 pad 1: Net-(D4-Pad1) -> GND
- D4 pad 2: Net-(D4-Pad2) -> VBUS
- D5 pad 1: /Processor/3V3_CORE_EN -> Net-(D5-Pad1)
- D5 pad 2: /Processor/USR_BTN.PWR -> GND
- D6 pad 1: Net-(D6-Pad1) -> /Power/PWR_CTRL.CORE_EN
- D6 pad 2: Net-(C62-Pad2) -> /Display B2B/USR_BTN.PWR
- D7 pad 2: VDD_AUX_3V3 -> 3V3_CORE
- D8 pad 2: 3V3_CORE -> VDD_AUX_3V3
- H1 pad 1: Net-(H1-Pad1) -> GND
- H2 pad 1: Net-(H2-Pad1) -> GND
- J2 pad 1: /Power/PAC1934.SCL -> GND
- J2 pad 2: /Power/PAC1934.SDA -> GND
- J3 pad A4: Net-(C36-Pad1) -> VBUS
- J3 pad A6: Net-(J1-PadA6) -> /USB/PORT_D+
- J3 pad A7: Net-(J1-PadA7) -> /USB/PORT_D-
- J3 pad A9: Net-(C36-Pad1) -> VBUS
- J3 pad B4: Net-(C36-Pad1) -> VBUS
- J3 pad B6: Net-(J1-PadA6) -> /USB/PORT_D+
- J3 pad B7: Net-(J1-PadA7) -> /USB/PORT_D-
- J3 pad B9: Net-(C36-Pad1) -> VBUS
- J3 pad S1: Net-(J1-PadS1) -> GND
- J4 pad 1: GND -> Net-(J4-Pad1)
- J4 pad 10: GND -> Net-(J4-Pad10)
- J4 pad 12: GND -> (no net)
- J4 pad 2: GND -> Net-(J4-Pad2)
- J4 pad 3: GND -> Net-(J4-Pad3)
- J4 pad 4: GND -> VDD_AUX_3V3
- J4 pad 5: VCC_BKUP_3V3 -> Net-(J4-Pad5)
- J4 pad 6: VDD_NVDC -> GND
- J4 pad 7: VCC_BKUP_3V3 -> Net-(J4-Pad7)
- J4 pad 8: VDD_NVDC -> Net-(J4-Pad8)
- L2 pad 1: VCC_BKUP_3V3 -> Net-(C9-Pad1)
- L2 pad 2: /Processor/3V3_ESP_BCKP_FILT -> Net-(AE1-Pad1)
- L3 pad 1: 3V3_CORE -> Net-(C22-Pad2)
- L3 pad 2: /Processor/3V3_ESP_CORE_FILT -> VDD_NVDC
- L4 pad 1: Net-(C15-Pad1) -> Net-(L4-Pad1)
- L4 pad 2: Net-(AE1-Pad2) -> VDD_SYS_3V3
- Q2 pad 3: /Processor/DEV_BTN.RST -> /Processor/DEV_BTN.BOOT
- Q3 pad 2: Net-(Q3-Pad2) -> /Power/PWR_CTRL.CORE_EN
- Q3 pad 3: /Processor/DEV_BTN.BOOT -> GND
- Q4 pad 1: /GPS/L96_1PPS -> Net-(Q4-Pad1)
- Q4 pad 2: GND -> /Power/PWR_CTRL.AUX_EN
- Q4 pad 3: Net-(D3-Pad1) -> GND
- R10 pad 1: Net-(R10-Pad1) -> /GPS/L96_RXD
- R10 pad 2: GND -> /GPS/GPS_UART.TX
- R11 pad 1: Net-(R11-Pad1) -> /Processor/USB_PRESENT
- R11 pad 2: /Processor/USB_PRESENT -> 3V3_CORE
- R12 pad 1: Net-(R12-Pad1) -> Net-(D3-Pad1)
- R12 pad 2: /BMS/CHARGE_STAT -> /Processor/USB_PRESENT
- R13 pad 1: Net-(R11-Pad1) -> Net-(D2-Pad1)
- R13 pad 2: 3V3_CORE -> Net-(R13-Pad2)
- R14 pad 1: Net-(D2-Pad1) -> Net-(R14-Pad1)
- R14 pad 2: Net-(R11-Pad1) -> GND
- R15 pad 1: Net-(R12-Pad1) -> Net-(R15-Pad1)
- R15 pad 2: 3V3_CORE -> GND
- R16 pad 1: Net-(D1-Pad1) -> /BMS/THERM_SHDN
- R16 pad 2: Net-(R12-Pad1) -> Net-(R15-Pad1)
- R17 pad 1: Net-(R17-Pad1) -> +BATT
- R17 pad 2: GND -> /BMS/I_{bat}.-
- R18 pad 1: /BMS/CHARGE_SHDN -> 3V3_CORE
- R18 pad 2: GND -> /BMS/SENSOR_I2C.SDA
- R19 pad 1: /BMS/THERM_SHDN -> 3V3_CORE
- R19 pad 2: /BMS/CHARGE_SHDN -> /BMS/SENSOR_I2C.SCL
- R2 pad 1: VCC_BKUP_3V3 -> Net-(R2-Pad1)
- R2 pad 2: /Processor/DEV_BTN.RST -> GND
- R20 pad 1: +BATT -> 3V3_CORE
- R20 pad 2: unconnected-(R20-Pad2) -> Net-(R20-Pad2)
- R21 pad 1: Net-(R21-Pad1) -> /USB/PORT_D-
- R21 pad 2: +BATT -> /USB/TERM_PORT_D-
- R22 pad 1: 3V3_CORE -> /USB/PORT_D+
- R22 pad 2: /BMS/SENSOR_I2C.SDA -> /USB/TERM_PORT_D+
- R23 pad 1: 3V3_CORE -> Net-(D5-Pad1)
- R23 pad 2: /BMS/SENSOR_I2C.SCL -> VBUS
- R24 pad 1: 3V3_CORE -> Net-(Q1-Pad1)
- R24 pad 2: Net-(R24-Pad2) -> VDD_USB_3V3
- R25 pad 1: Net-(R25-Pad1) -> /USB/CP2102N_D-
- R25 pad 2: +BATT -> /USB/TERM_CP2102N_D-
- R26 pad 1: GND -> /USB/CP2102N_D+
- R26 pad 2: Net-(R25-Pad1) -> /USB/TERM_CP2102N_D+
- R27 pad 1: Net-(R27-Pad1) -> Net-(Q1-Pad1)
- R27 pad 2: +BATT -> VDD_USB_3V3
- R28 pad 1: GND -> Net-(R28-Pad1)
- R28 pad 2: Net-(R27-Pad1) -> VDD_USB_3V3
- R29 pad 2: +BATT -> GND
- R3 pad 1: Net-(R3-Pad1) -> VDD_AUX_3V3
- R3 pad 2: GND -> /BMS/SENSOR_I2C.SDA
- R30 pad 1: GND -> Net-(Q2-Pad2)
- R30 pad 2: Net-(R29-Pad1) -> Net-(Q2-Pad4)
- R31 pad 1: Net-(J1-PadS1) -> Net-(Q2-Pad1)
- R31 pad 2: GND -> Net-(Q2-Pad5)
- R32 pad 1: Net-(J1-PadA7) -> Net-(R32-Pad1)
- R32 pad 2: Net-(R32-Pad2) -> VDD_USB_3V3
- R33 pad 1: Net-(J1-PadA6) -> 3V3_CORE
- R34 pad 1: /Processor/USB_PRESENT -> VCC_BKUP_3V3
- R34 pad 2: VDD_USB_3V3 -> Net-(Q3-Pad1)
- R35 pad 1: Net-(R35-Pad1) -> VCC_BKUP_3V3
- R35 pad 2: /Processor/USB_PRESENT -> Net-(R35-Pad2)
- R36 pad 1: Net-(Q1-Pad1) -> VDD_SYS_3V3
- R36 pad 2: VDD_USB_3V3 -> /Power/PWR_CTRL.CORE_EN
- R37 pad 1: Net-(Q1-Pad1) -> VDD_SYS_3V3
- R37 pad 2: Net-(R35-Pad1) -> Net-(C47-Pad2)
- R38 pad 1: Net-(R38-Pad1) -> Net-(C47-Pad2)
- R38 pad 2: Net-(Q1-Pad1) -> GND
- R39 pad 1: Net-(R39-Pad1) -> VCC_BKUP_3V3
- R4 pad 2: /BMS/SENSOR_I2C.SDA -> /BMS/SENSOR_I2C.SCL
- R40 pad 1: Net-(R40-Pad1) -> 3V3_CORE
- R41 pad 1: VDD_USB_3V3 -> GND
- R41 pad 2: Net-(R41-Pad2) -> Net-(D7-Pad1)
- R42 pad 1: Net-(R38-Pad1) -> VDD_SYS_3V3
- R42 pad 2: Net-(R41-Pad2) -> Net-(Q4-Pad1)
- R43 pad 1: Net-(R43-Pad1) -> VDD_AUX_3V3
- R43 pad 2: VDD_USB_3V3 -> Net-(R43-Pad2)
- R44 pad 1: /Processor/DEBUG_UART.RXD -> GND
- R44 pad 2: /USB/CP2102N_UART_TX -> Net-(D8-Pad1)
- R45 pad 1: /Processor/DEBUG_UART.TXD -> /Processor/SDMMC.D2
- R45 pad 2: /USB/CP2102N_UART_RX -> Net-(J4-Pad1)
- R46 pad 1: 3V3_CORE -> /Processor/SDMMC.D3
- R46 pad 2: Net-(R46-Pad2) -> Net-(J4-Pad2)
- R47 pad 1: Net-(Q2-Pad1) -> /Processor/SDMMC.CMD
- R47 pad 2: Net-(Q3-Pad2) -> Net-(J4-Pad3)
- R48 pad 1: Net-(Q2-Pad2) -> /Processor/SDMMC.CLK
- R48 pad 2: Net-(Q3-Pad1) -> Net-(J4-Pad5)
- R49 pad 1: Net-(D3-Pad2) -> /Processor/SDMMC.D0
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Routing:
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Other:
- copper layers 2 -> 4
- rule pad_to_mask_clearance: 0 -> 0.05
